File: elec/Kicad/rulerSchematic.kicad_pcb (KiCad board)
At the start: 2 copper layers, 30.1 x 155 mm, 121 parts, among them J1 USART, J2 B2B-XH-A, J3 HX0201800000G, J4 Conn_01x05, J5 TestPoint, J6 SWD, J7 USB_B_Micro_MAIN, J8 SD_CARD_CONN, J9 Conn_01x13, Q1 SI2323DS-T1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

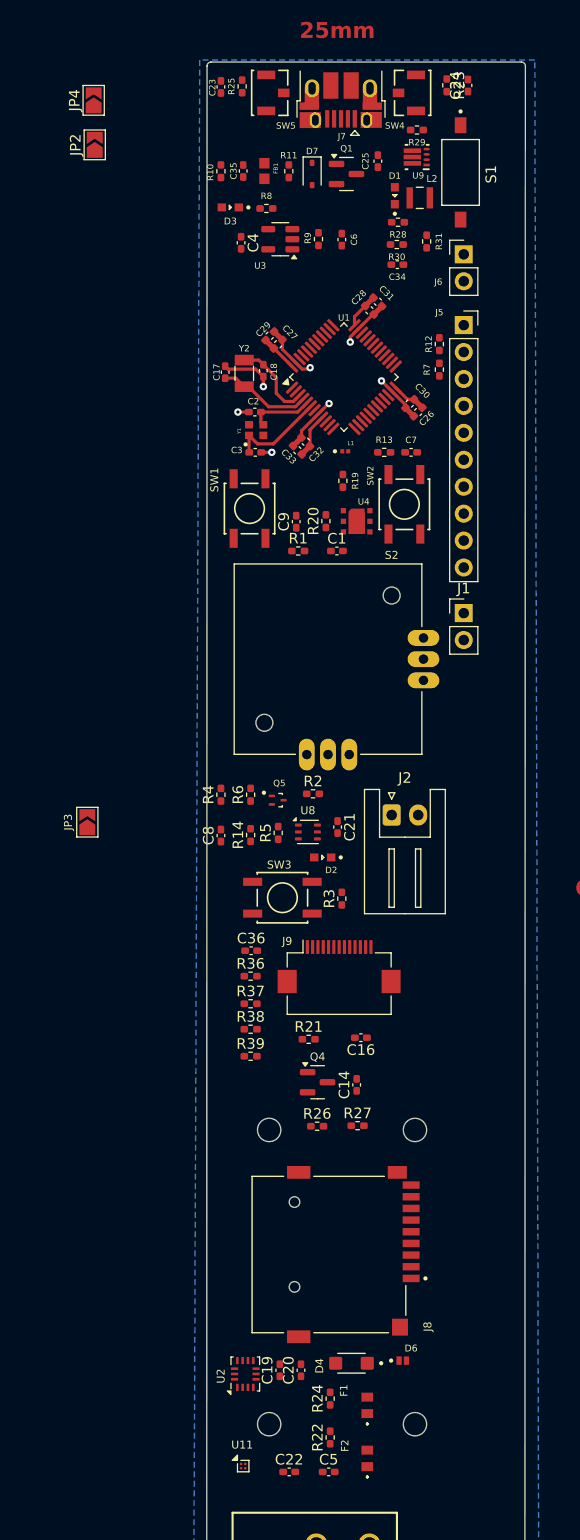
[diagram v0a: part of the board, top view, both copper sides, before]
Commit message: modification du magnéto
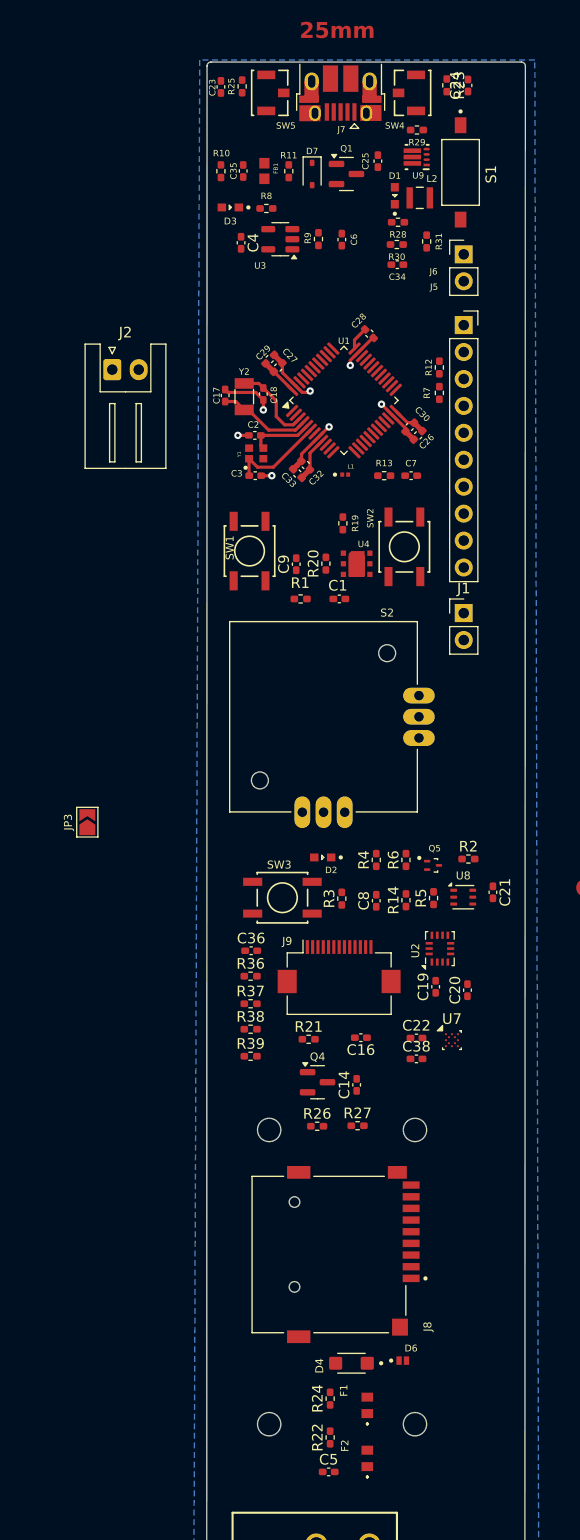
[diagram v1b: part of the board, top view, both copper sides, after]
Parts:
- removed C31: 100nF, Capacitor_SMD:C_0402_1005Metric_Pad0.74x0.62mm_HandSolder
- removed JP2: USB_ID, Jumper:SolderJumper-2_P1.3mm_Open_TrianglePad1.0x1.5mm
- removed JP4: USB_SHIELD, Jumper:SolderJumper-2_P1.3mm_Open_TrianglePad1.0x1.5mm
- removed U11: MMC5633NJL, Package_BGA:WLP-4_0.86x0.86mm_P0.4mm
- added C38: 100nF, Capacitor_SMD:C_0402_1005Metric_Pad0.74x0.62mm_HandSolder, F.Cu at (70.6, 126.8)
- added U7: BMM150, Package_CSP:WLCSP-12_1.56x1.56mm_P0.4mm, F.Cu at (74.0, 125.0)
- C22: value 2.2uF -> 100nF
- moved J2 49.6 mm to (42.0, 61.8)
- moved U2 44.1 mm to (72.8, 116.4)
- moved C22 42.6 mm to (70.6, 124.8)
- moved C20 39.1 mm to (75.5, 120.3)
- moved C19 39.0 mm to (72.5, 120.0)
- moved R14 15.9 mm to (69.7, 111.8)
- moved R5 15.9 mm to (72.2, 111.6)
- moved R6 15.9 mm to (69.7, 108.0)
- moved Q5 15.9 mm to (72.2, 108.5)
- moved U8 15.9 mm to (75.0, 111.5)
- moved C21 15.9 mm to (77.8, 111.1)
- moved C8 15.9 mm to (66.8, 111.9)
- moved R2 15.9 mm to (75.5, 108.0)
- moved R4 15.9 mm to (66.8, 108.0)
- moved S2 5.45 mm to (61.9, 94.5)
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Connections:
- C22 pad 1: +3.3V -> GND
- C22 pad 2: GND -> +3.3V
- J7 pad 4: Net-(J7-ID) -> unconnected-(J7-ID-Pad4)
- J7 pad 6: Net-(J7-Shield) -> GND
- U1 pad 2: unconnected-(U1-PC13-Pad2) -> RESET_LCD
- U1 pad 39: RESET_LCD -> unconnected-(U1-PB3-Pad39)
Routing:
- net +3.3V: track 10.2 -> 9.09 mm
- net GND: track 27.3 -> 26.2 mm
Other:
- board text added: "Acheter un Stencil"

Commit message: abdel aziz clutch l'app5
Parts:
- removed C22, C38: 100nF, Capacitor_SMD:C_0402_1005Metric_Pad0.74x0.62mm_HandSolder
- removed JP1: SolderJumper_2_Open, Jumper:SolderJumper-2_P1.3mm_Open_TrianglePad1.0x1.5mm
- removed JP3: Bypass_MOSFET, Jumper:SolderJumper-2_P1.3mm_Open_TrianglePad1.0x1.5mm
- removed U7: BMM150, Package_CSP:WLCSP-12_1.56x1.56mm_P0.4mm
- added J10: Conn_01x06, Connector_PinSocket_2.54mm:PinSocket_1x06_P2.54mm_Vertical, F.Cu at (143.3, 165.1)
- added R18: Bypass_MOSFET (0 ohm), Resistor_SMD:R_0201_0603Metric, F.Cu at (151.2, 33.8)
- added R32: Bypass_XSHUT (0 ohm), Resistor_SMD:R_0402_1005Metric_Pad0.72x0.64mm_HandSolder, F.Cu at (142.3, 173.0)
- added R33: 10K, Resistor_SMD:R_0402_1005Metric_Pad0.72x0.64mm_HandSolder, F.Cu at (149.9, 90.4)
- added mouse-bite-3mm-slot: VAL**, PanelizationMouseBite:mouse-bite-3mm-slot, F.Cu at (150.1, 169.4)
- J2: value B2B-XH-A -> S2B-XH-A; moved to B.Cu
- J4: value Conn_01x05 -> Conn_01x06; footprint Connector_PinSocket_2.54mm:PinSocket_1x05_P2.54mm_Vertical -> Connector_PinHeader_2.54mm:PinHeader_1x06_P2.54mm_Horizontal
- U2: value BMI160 -> ADXL343BCCZ; footprint Package_LGA:Bosch_LGA-14_3x2.5mm_P0.5mm -> ADXL343:LGA_CC-14-1_ADI
- moved Q2 179.2 mm to (148.4, 178.5), turned to -90 degrees
- moved Q3 177.8 mm to (144.4, 178.6), turned to -90 degrees
- moved C10 167.4 mm to (144.4, 173.1), turned to -90 degrees
- moved R16 167.3 mm to (144.6, 175.5)
- moved R15 167.3 mm to (148.8, 175.9), turned to 180 degrees
- moved U6 165.5 mm to (155.5, 178.3), turned to 180 degrees
- moved C11 164.3 mm to (145.9, 173.1), turned to -90 degrees
- moved C13 160.6 mm to (152.4, 178.3), turned to 90 degrees
- moved U5 159.7 mm to (150.1, 173.2)
- moved C12 158.7 mm to (158.6, 177.3), turned to -90 degrees
- moved R17 156.9 mm to (155.0, 173.3), turned to 90 degrees
- moved C15 156.6 mm to (158.6, 179.9), turned to -90 degrees
- moved R20 136.8 mm to (153.0, 182.3), turned to 180 degrees
- moved R19 136.6 mm to (149.8, 182.3), turned to 180 degrees
- moved R4 112.8 mm to (148.5, 30.2), turned to 0 degrees
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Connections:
- J1 pad 1: USART1_TX -> USART1_RX
- J1 pad 2: USART1_RX -> USART1_TX
- J4 pad 2: I2C1_SCL -> +2V8
- J4 pad 4: XSHUT -> I2C1_SCL
- J4 pad 5: GND -> XSHUT
- J5 pad 1: +2V8 -> +5V
- J5 pad 2: +3.3V -> Vbat
- J5 pad 3: +5V -> +3.3V
- J5 pad 4: BAT_PERCENT -> +2V8
- J5 pad 7: SPI1_SCK -> SPI1_MOSI
- J5 pad 9: SPI1_MOSI -> SPI1_SCK
- J6 pad 1: SWDIO -> SWCLK
- J6 pad 2: SWCLK -> SWDIO
- U1 pad 11: /MCU and power management/LED_STAT -> JOYSTICK_Y
- U1 pad 13: JOYSTICK_Y -> read_pin
- U1 pad 18: read_pin -> RESET_LCD
- U1 pad 2: RESET_LCD -> unconnected-(U1-PC13-Pad2)
- U1 pad 21: PB10_Bouton_BACK -> PB11_Bouton_IN
- U1 pad 22: PB11_Bouton_IN -> PB10_Bouton_BACK
- U1 pad 39: unconnected-(U1-PB3-Pad39) -> /MCU and power management/LED_STAT
- U2 pad 1: GND -> +3.3V
- U2 pad 12: unconnected-(U2-CSB-Pad12) -> +3.3V
- U2 pad 13: I2C1_SCL -> I2C1_SDA
- U2 pad 14: I2C1_SDA -> I2C1_SCL
- U2 pad 2: unconnected-(U2-ASDx-Pad2) -> GND
- U2 pad 4: unconnected-(U2-INT1-Pad4) -> GND
- U2 pad 5: +3.3V -> GND
- U2 pad 6: GND -> +3.3V
- U2 pad 7: GND -> +3.3V
- U2 pad 8: +3.3V -> unconnected-(U2-INT1-Pad8)
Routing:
- net +3.3V: track 9.09 -> 537.6 mm, vias 0 -> 6
- net +2V8: track 0.00 -> 178.0 mm, vias 0 -> 3
- net I2C1_SCL: track 0.00 -> 172.3 mm, vias 0 -> 3
- net I2C1_SDA: track 0.00 -> 171.5 mm, vias 0 -> 5
- net XSHUT: track 0.00 -> 151.5 mm, vias 0 -> 3
- net SPI1_MOSI: track 0.00 -> 103.1 mm, vias 0 -> 2
- net SPI1_SCK: track 0.00 -> 100.5 mm, vias 0 -> 3
- net read_pin: track 0.00 -> 98.1 mm, vias 0 -> 2
- net CS_SD: track 0.00 -> 96.3 mm, vias 0 -> 4
- net SPI1_MISO: track 0.00 -> 86.9 mm, vias 0 -> 2
- net BL_LCD: track 0.00 -> 67.9 mm, vias 0 -> 2
- net RS_LCD: track 0.00 -> 58.6 mm, vias 0 -> 2
- net NRST: track 0.00 -> 57.9 mm, vias 0 -> 2
- net RESET_LCD: track 0.00 -> 56.4 mm, vias 0 -> 2
- net CS_LCD: track 0.00 -> 54.7 mm, vias 0 -> 2
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- added copper zone on F.Cu, net GND
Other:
- board size 30.1 x 155 mm -> 30.1 x 173.7 mm
- board text added: "0"
- board text added: "1"
- board text added: "10"
- board text added: "11"
- board text added: "12"
- board text added: "13"
- board text added: "14"
- board text added: "15"
- board text added: "2"
- board text added: "3"
- board text added: "4"
- board text added: "5"
- board text added: "6"
- board text added: "7"
- board text added: "8"
- board text added: "9"
- board text added: "Le TouilloMètre"
- board text removed: "20mm"
- board text removed: "25mm"
- board text removed: "30mm"
- board text removed: "Changer le connecteur de la batterie pour le :S2B-XH-A-1"

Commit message: j'essaye de fix la hauteur des designator pis si sa scrap cv être ça
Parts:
- J10: value Conn_01x06 -> TouillomètreMount
- J4: value Conn_01x06 -> ToFMount
- L1: footprint LQP03TN27NJ02D:INDC0603X33N -> LQG15HN27NJ02D:INDC1005X55N
- moved R32 14.0 mm to (156.3, 173.2)
- moved L1 1.90 mm to (142.1, 52.5), turned to 0 degrees
- moved R17 0.69 mm to (154.3, 173.2)
- moved J7 0.51 mm to (147.9, 16.3)
- moved C10 0.38 mm to (144.4, 173.4)
- moved C11 0.29 mm to (145.9, 173.4)
- moved R10 0.26 mm to (140.1, 24.0)
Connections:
- C12 pad 1: +3.3V -> +3V3
- C15 pad 1: +3.3V -> +3V3
- J4 pad 1: +3.3V -> +3V3
- J4 pad 3: I2C1_SDA -> I2C_SDA
- J4 pad 4: I2C1_SCL -> I2C_SCL
- J4 pad 5: XSHUT -> XSHUT_Breakout
- Q2 pad 3: I2C1_SDA -> I2C_SDA
- Q3 pad 3: I2C1_SCL -> I2C_SCL
- R17 pad 1: XSHUT -> XSHUT_Breakout
- R19 pad 1: +3.3V -> +3V3
- R19 pad 2: I2C1_SCL -> I2C_SCL
- R20 pad 1: +3.3V -> +3V3
- R20 pad 2: I2C1_SDA -> I2C_SDA
- U6 pad 1: +3.3V -> +3V3
- U6 pad 3: +3.3V -> +3V3
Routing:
- net GND: track 22.7 -> 98.5 mm, vias 217 -> 80
- net +3V3: track 0.00 -> 27.5 mm
- net +3.3V: track 537.6 -> 512.9 mm
- net XSHUT_Breakout: track 0.00 -> 16.7 mm, vias 0 -> 1
- net XSHUT: track 151.5 -> 137.0 mm, vias 3 -> 2
- net I2C_SDA: track 0.00 -> 9.09 mm, vias 0 -> 2
- net I2C1_SDA: track 171.5 -> 162.4 mm, vias 5 -> 3
- net I2C1_SCL: track 172.3 -> 163.6 mm
- net I2C_SCL: track 0.00 -> 8.68 mm
- net +2V8: track 178.0 -> 184.6 mm
- net VinBat: track 17.9 -> 23.2 mm
- net Net-(U5-XSHUT): track 3.39 -> 4.66 mm
- net JOYSTICK_X: track 42.8 -> 43.9 mm
- net JOYSTICK_Y: track 44.3 -> 45.3 mm
- net +5V: track 33.9 -> 33.2 mm
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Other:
- board text added: "3V3"
- board text added: "GND"
- board text removed: "Air de Touillomètre: 15.5*2.5 = 38.75cm²"
- board text removed: "Air max: 15.5*3 = 46.5cm²"
- board text removed: "POUR LES TRACES: CEUX DE POWER : UTILISER LES 0.5mm CEUX DE SIGNAUX : UTILISER LES 0.3mm"
- board text removed: "Petit PCB pour ça"
